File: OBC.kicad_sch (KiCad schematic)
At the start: 11 parts, among them J1 I2C, J2 Conn_02x07_Counter_Clockwise, J6 SWD, J7 RMF, SW3 SW_Push, SW5 RST, U1 E73-2G4M08S1C, Y1 32.768

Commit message: Started PCB layout
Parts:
- removed J2: Conn_02x07_Counter_Clockwise, symbol Connector_Generic:Conn_02x07_Counter_Clockwise
- added J8: GPIO, Connector_PinHeader_2.54mm:PinHeader_2x07_P2.54mm_Vertical, symbol Connector_Generic:Conn_02x07_Odd_Even
- J1: footprint (none) -> Connector_PinHeader_2.54mm:PinHeader_1x04_P2.54mm_Vertical
- L1: footprint Inductor_SMD:L_Changjiang_FTC201610D -> Inductor_SMD:L_1210_3225Metric
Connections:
- net +3.3V: now also J8.2 (Pin_2)
- net GND: now also J8.4 (Pin_4)
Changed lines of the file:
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@@
+		)
+	)
+	(global_label "RMF"
+		(shape input)
+		(at 68.58 115.57 0)
+		(fields_autoplaced yes)
+		(effects
+			(font
+				(size 1.27 1.27)
+			)
+			(justify left)
+		)
+		(property "Intersheetrefs" "${INTERSHEET_REFS}"
+			(at 75.3752 115.57 0)
+			(hide yes)
+			(show_name no)
+			(do_not_autoplace no)
+			(effects
+				(font
+					(size 1.27 1.27)
+				)
+				(justify left)
+			)
 		)
 	)
@@
 		)
 	)
+	(global_label "RMF"
+		(shape input)
+		(at 250.19 133.35 180)
+		(fields_autoplaced yes)
+		(effects
+			(font
+				(size 1.27 1.27)
+			)
+			(justify right)
+		)
+		(property "Intersheetrefs" "${INTERSHEET_REFS}"
+			(at 243.3948 133.35 0)
+			(hide yes)
+			(show_name no)
+			(do_not_autoplace no)
+			(effects
+				(font
+					(size 1.27 1.27)
+				)
+				(justify right)
+			)
+		)
+	)
 	(global_label "LoRa_SCK"
 		(shape input)
@@
 		)
 	)
-	(hierarchical_label "RMF"
-		(shape input)
-		(at 68.58 115.57 0)
-		(effects
-			(font
-				(size 1.27 1.27)
-			)
-			(justify left)
-		)
-	)
 	(hierarchical_label "{LoRa_BUS}"
 		(shape input)
@@
 			)
 			(justify left)
-		)
-	)
-	(hierarchical_label "RMF"
-		(shape input)
-		(at 250.19 133.35 180)
-		(effects
-			(font
-				(size 1.27 1.27)
-			)
-			(justify right)
 		)
 	)
@@
 	)
 	(symbol
+		(lib_id "Connector_Generic:Conn_02x07_Odd_Even")
+		(at 135.89 125.73 0)
+		(unit 1)
+		(body_style 1)
+		(exclude_from_sim no)
+		(in_bom yes)
+		(on_board yes)
+		(in_pos_files yes)
+		(dnp no)
+		(fields_autoplaced yes)
+		(property "Reference" "J8"
+			(at 137.16 111.76 0)
+			(show_name no)
+			(do_not_autoplace no)
+			(effects
+				(font
+					(size 1.27 1.27)
+				)
+			)
+		)
+		(property "Value" "GPIO"
+			(at 137.16 114.3 0)
+			(show_name no)
+			(do_not_autoplace no)
+			(effects
+				(font
+					(size 1.27 1.27)
+				)
+			)
+		)
+		(property "Footprint" "Connector_PinHeader_2.54mm:PinHeader_2x07_P2.54mm_Vertical"
+			(at 135.89 125.73 0)
+			(hide yes)
+			(show_name no)
+			(do_not_autoplace no)
+			(effects
+				(font
+					(size 1.27 1.27)
+				)
+			)
+		)
+		(property "Datasheet" ""
+			(at 135.89 125.73 0)
+			(hide yes)
+			(show_name no)
+			(do_not_autoplace no)
+			(effects
+				(font
+					(size 1.27 1.27)
+				)
+			)
+		)
+		(property "Description" "Generic connector, double row, 02x07, odd/even pin numbering scheme (row 1 odd numbers, row 2 even numbers), script generated (kicad-library-utils/schlib/autogen/connector/)"
+			(at 135.89 125.73 0)
+			(hide yes)
+			(show_name no)
+			(do_not_autoplace no)
+			(effects
+				(font
+					(size 1.27 1.27)
+				)
+			)
+		)
+		(pin "14"
+		)
+		(pin "13"
+		)
+		(pin "12"
+		)
+		(pin "11"
+		)
+		(pin "10"
+		)
+		(pin "1"
+		)
+		(pin "3"
+		)
+		(pin "2"
+		)
+		(pin "4"
+		)
+		(pin "6"
+		)
+		(pin "7"
+		)
+		(pin "5"
+		)
+		(pin "9"
+		)
+		(pin "8"
+		)
+		(instances
+			(project "CanSat_Devboard"
+				(path "/f9e05184-c88b-4a88-ae9c-ab2bdb32be7c/5d00bd0a-3bbf-46b2-b8c5-f75441fb4350/2028456c-6ef4-4d71-987d-d023cb9d3da5"
+					(reference "J8")
+					(unit 1)
+				)
+			)
+		)
+	)
+	(symbol
 		(lib_id "power:GND")
 		(at 256.54 100.33 90)
@@
 			)
 		)
-		(property "Footprint" "Inductor_SMD:L_Changjiang_FTC201610D"
+		(property "Footprint" "Inductor_SMD:L_1210_3225Metric"
 			(at 73.66 127 0)
 			(hide yes)
@@
 			)
 		)
-		(property "Footprint" ""
+		(property "Footprint" "Connector_PinHeader_2.54mm:PinHeader_1x04_P2.54mm_Vertical"
 			(at 191.77 127 0)
 			(hide yes)
@@
 					(unit 1)
 				)
-			)
-		)
-	)
-	(symbol
-		(lib_id "Connector_Generic:Conn_02x07_Counter_Clockwise")
-		(at 135.89 125.73 0)
-		(unit 1)
-		(body_style 1)
-		(exclude_from_sim no)
-		(in_bom yes)
-		(on_board yes)
-		(in_pos_files yes)
-		(dnp no)
-		(fields_autoplaced yes)
-		(property "Reference" "J2"
-			(at 137.16 111.76 0)
-			(show_name no)
-			(do_not_autoplace no)
-			(effects
-				(font
-					(size 1.27 1.27)
-				)
-			)
-		)
-		(property "Value" "Conn_02x07_Counter_Clockwise"
-			(at 137.16 114.3 0)
-			(show_name no)
-			(do_not_autoplace no)
-			(effects
-				(font
-					(size 1.27 1.27)
-				)
-			)
-		)
-		(property "Footprint" ""
-			(at 135.89 125.73 0)
-			(hide yes)
-			(show_name no)
-			(do_not_autoplace no)
-			(effects
-				(font
-					(size 1.27 1.27)
-				)
-			)
-		)
-		(property "Datasheet" ""
-			(at 135.89 125.73 0)
-			(hide yes)
-			(show_name no)
-			(do_not_autoplace no)
-			(effects
-				(font
-					(size 1.27 1.27)
-				)
-			)
-		)
-		(property "Description" "Generic connector, double row, 02x07, counter clockwise pin numbering scheme (similar to DIP package numbering), script generated (kicad-library-utils/schlib/autogen/connector/)"
-			(at 135.89 125.73 0)
-			(hide yes)
-			(show_name no)
-			(do_not_autoplace no)
-			(effects
-				(font
-					(size 1.27 1.27)
-				)
-			)
-		)
-		(pin "1"
-		)
-		(pin "12"
-		)
-		(pin "2"
-		)
-		(pin "6"
-		)
-		(pin "7"
-		)
-		(pin "14"
-		)
-		(pin "3"
-		)
-		(pin "8"
-		)
-		(pin "9"
-		)
-		(pin "5"
-		)
-		(pin "13"
-		)
-		(pin "11"
-		)
-		(pin "4"
-		)
-		(pin "10"
-		)
-		(instances
-			(project "CanSat_Devboard"
-				(path "/f9e05184-c88b-4a88-ae9c-ab2bdb32be7c/5d00bd0a-3bbf-46b2-b8c5-f75441fb4350/2028456c-6ef4-4d71-987d-d023cb9d3da5"
-					(reference "J2")
-					(unit 1)
-				)

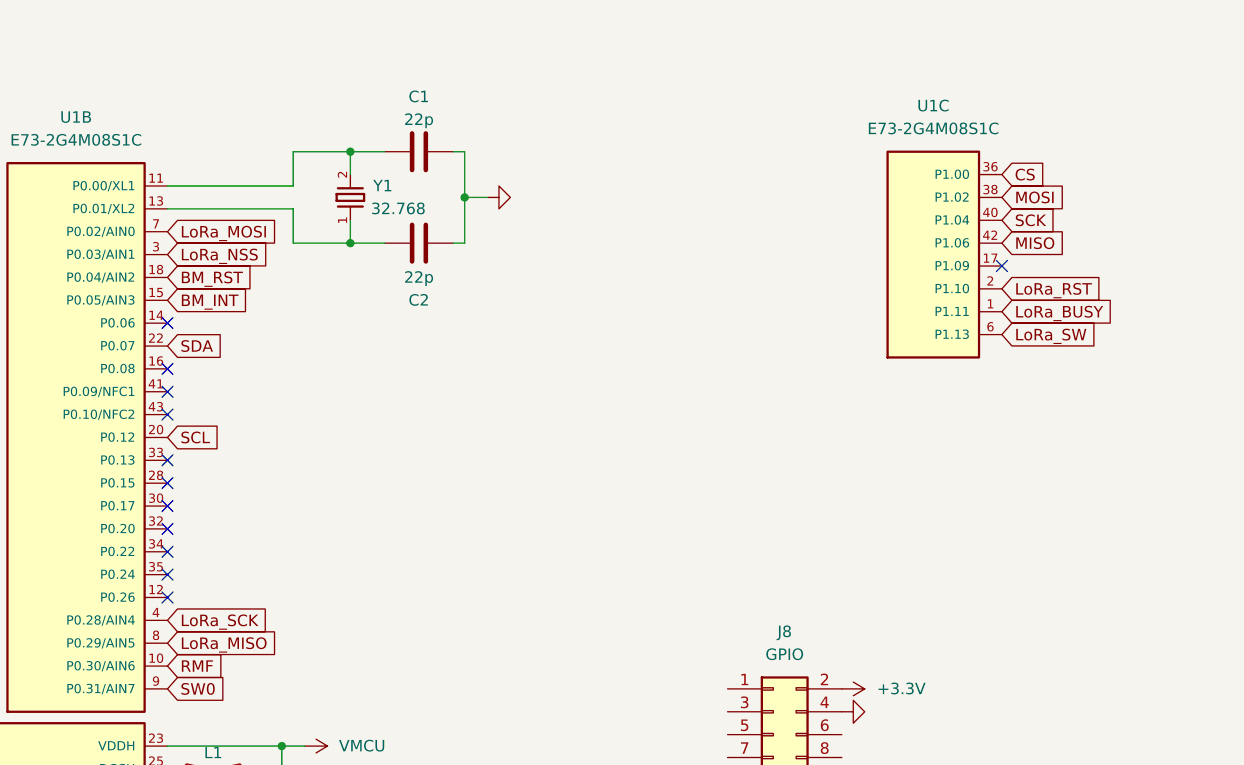
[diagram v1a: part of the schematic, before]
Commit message: Started layout
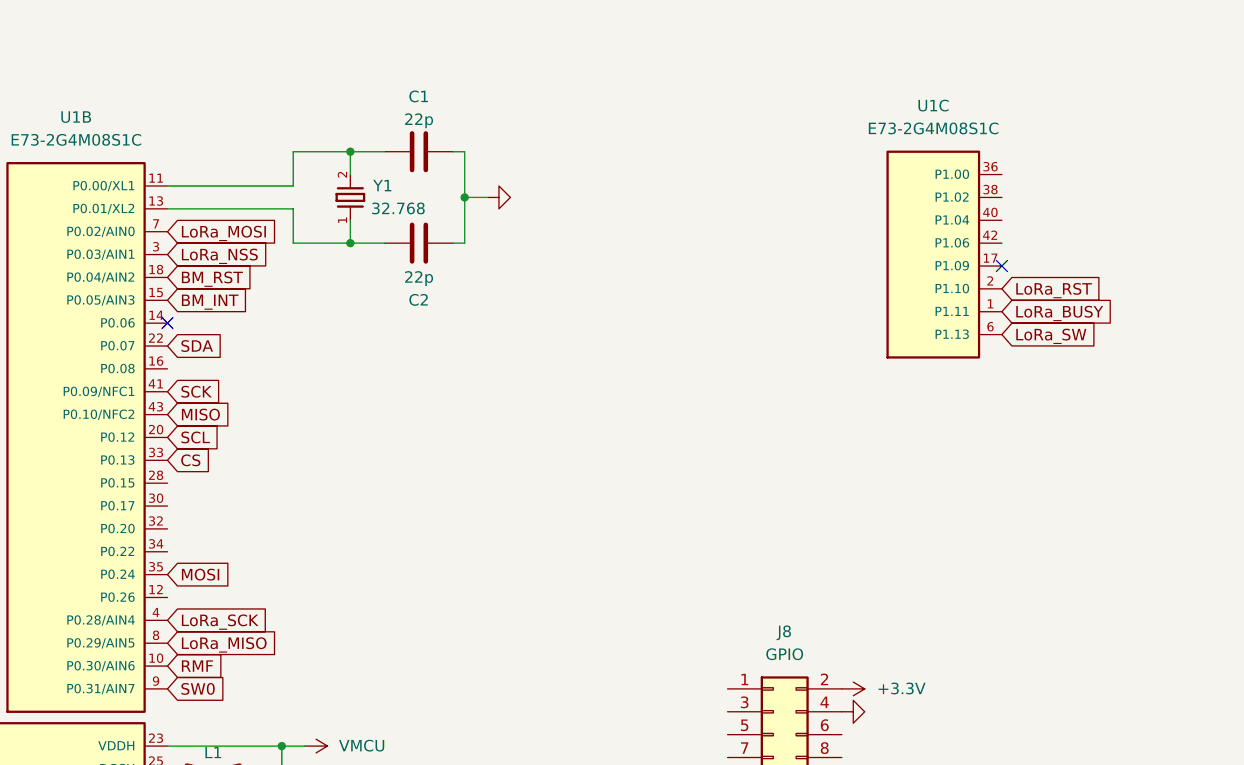
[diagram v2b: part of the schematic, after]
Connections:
- net CS: now also U1.33 (P0.13); no longer U1.36 (P1.00)
- net MISO: now also U1.43 (P0.10/NFC2); no longer U1.42 (P1.06)
- net MOSI: now also U1.35 (P0.24); no longer U1.38 (P1.02)
- net SCK: now also U1.41 (P0.09/NFC1); no longer U1.40 (P1.04)
- no-connect marks 13 -> 3
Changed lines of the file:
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@@
-	)
-	(no_connect
-		(at 68.58 92.71)
-	)
-	(no_connect
-		(at 68.58 107.95)
 	)
 	(no_connect
@@
 	)
 	(no_connect
-		(at 68.58 95.25)
-	)
-	(no_connect
 		(at 161.29 71.12)
-	)
-	(no_connect
-		(at 68.58 100.33)
-	)
-	(no_connect
-		(at 68.58 82.55)
 	)
 	(no_connect
 		(at 256.54 119.38)
 	)
-	(no_connect
-		(at 68.58 87.63)
-	)
-	(no_connect
-		(at 68.58 102.87)
-	)
-	(no_connect
-		(at 68.58 105.41)
-	)
-	(no_connect
-		(at 68.58 85.09)
-	)
-	(no_connect
-		(at 68.58 97.79)
-	)
 	(bus_entry
 		(at 217.17 46.99)
@@
 	(global_label "MOSI"
 		(shape input)
-		(at 161.29 63.5 0)
-		(fields_autoplaced yes)
-		(effects
-			(font
-				(size 1.27 1.27)
-			)
-			(justify left)
-		)
-		(property "Intersheetrefs" "${INTERSHEET_REFS}"
-			(at 168.8714 63.5 0)
+		(at 68.58 105.41 0)
+		(fields_autoplaced yes)
+		(effects
+			(font
+				(size 1.27 1.27)
+			)
+			(justify left)
+		)
+		(property "Intersheetrefs" "${INTERSHEET_REFS}"
+			(at 76.1614 105.41 0)
 			(hide yes)
 			(show_name no)
@@
 	(global_label "MISO"
 		(shape input)
-		(at 161.29 68.58 0)
-		(fields_autoplaced yes)
-		(effects
-			(font
-				(size 1.27 1.27)
-			)
-			(justify left)
-		)
-		(property "Intersheetrefs" "${INTERSHEET_REFS}"
-			(at 168.8714 68.58 0)
+		(at 68.58 87.63 0)
+		(fields_autoplaced yes)
+		(effects
+			(font
+				(size 1.27 1.27)
+			)
+			(justify left)
+		)
+		(property "Intersheetrefs" "${INTERSHEET_REFS}"
+			(at 76.1614 87.63 0)
 			(hide yes)
 			(show_name no)
@@
 	(global_label "SCK"
 		(shape input)
-		(at 161.29 66.04 0)
-		(fields_autoplaced yes)
-		(effects
-			(font
-				(size 1.27 1.27)
-			)
-			(justify left)
-		)
-		(property "Intersheetrefs" "${INTERSHEET_REFS}"
-			(at 168.0247 66.04 0)
+		(at 68.58 85.09 0)
+		(fields_autoplaced yes)
+		(effects
+			(font
+				(size 1.27 1.27)
+			)
+			(justify left)
+		)
+		(property "Intersheetrefs" "${INTERSHEET_REFS}"
+			(at 75.3147 85.09 0)
 			(hide yes)
 			(show_name no)
@@
 	(global_label "CS"
 		(shape input)
-		(at 161.29 60.96 0)
-		(fields_autoplaced yes)
-		(effects
-			(font
-				(size 1.27 1.27)
-			)
-			(justify left)
-		)
-		(property "Intersheetrefs" "${INTERSHEET_REFS}"
-			(at 166.7547 60.96 0)
-			(hide yes)
-			(show_name no)
+		(at 68.58 92.71 0)
+		(fields_autoplaced yes)
+		(effects
+			(font
+				(size 1.27 1.27)
+			)
+			(justify left)
+		)
+		(property "Intersheetrefs" "${INTERSHEET_REFS}"
+			(at 74.0447 92.71 0)
+			(hide yes)
+			(show_name no)

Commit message: Continued layout and routing
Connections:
- net BM_RST: now also U1.17 (P1.09); no longer U1.18 (P0.04/AIN2)
- net LoRa_MISO: now also U1.3 (P0.03/AIN1); no longer U1.8 (P0.29/AIN5)
- net LoRa_MOSI: now also U1.4 (P0.28/AIN4); no longer U1.7 (P0.02/AIN0)
- net LoRa_NSS: now also U1.8 (P0.29/AIN5); no longer U1.3 (P0.03/AIN1)
- net LoRa_RST: now also U1.7 (P0.02/AIN0); no longer U1.2 (P1.10)
- net LoRa_SCK: now also U1.6 (P1.13); no longer U1.4 (P0.28/AIN4)
- net LoRa_SW: now also U1.2 (P1.10); no longer U1.6 (P1.13)
- net RMF: now also U1.32 (P0.20); no longer U1.10 (P0.30/AIN6)
- net SCL: now also U1.10 (P0.30/AIN6); no longer U1.20 (P0.12)
- net SDA: now also U1.9 (P0.31/AIN7); no longer U1.22 (P0.07)
- net SW0: now also U1.34 (P0.22); no longer U1.9 (P0.31/AIN7)
- no-connect marks 3 -> 2

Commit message: Finished PCB design
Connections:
- net +3.3V: now also J1.1 (Pin_1), J8.1 (Pin_1); no longer J1.3 (Pin_3), J8.2 (Pin_2)
- net GND: now also J1.2 (Pin_2), J8.2 (Pin_2); no longer J1.4 (Pin_4), J8.4 (Pin_4)
- net RMF: now also U1.14 (P0.06); no longer U1.32 (P0.20)
- net SCL: now also J1.4 (Pin_4); no longer J1.1 (Pin_1)
- net SDA: now also J1.3 (Pin_3); no longer J1.2 (Pin_2)
- net SW0: now also U1.12 (P0.26); no longer U1.34 (P0.22)
- net 0.08: now reaches U1.16 (P0.08)
- net 0.08: now also J8.14 (Pin_14)
- net 0.04: now reaches U1.18 (P0.04/AIN2)
- net 0.04: now also J8.13 (Pin_13)
- net 0.12: now reaches U1.20 (P0.12)
- net 0.12: now also J8.12 (Pin_12)
- net 0.07: now reaches U1.22 (P0.07)
- net 0.07: now also J8.11 (Pin_11)
- net 0.15: now reaches U1.28 (P0.15)
- net 0.15: now also J8.10 (Pin_10)
- net 0.17: now reaches U1.30 (P0.17)
- net 0.17: now also J8.9 (Pin_9)
- net 1.06: now reaches J8.3 (Pin_3)
- net 1.06: now also U1.42 (P1.06)
- net 1.02: now reaches J8.5 (Pin_5)
- net 1.02: now also U1.38 (P1.02)
- net 1.00: now reaches J8.6 (Pin_6)
- net 1.00: now also U1.36 (P1.00)
- net 0.22: now reaches J8.7 (Pin_7)
- net 0.22: now also U1.34 (P0.22)
- net 0.20: now reaches J8.8 (Pin_8)
- net 0.20: now also U1.32 (P0.20)
- net 1.04: now reaches U1.40 (P1.04)
- net 1.04: now also J8.4 (Pin_4)
- no-connect marks 2 -> 1

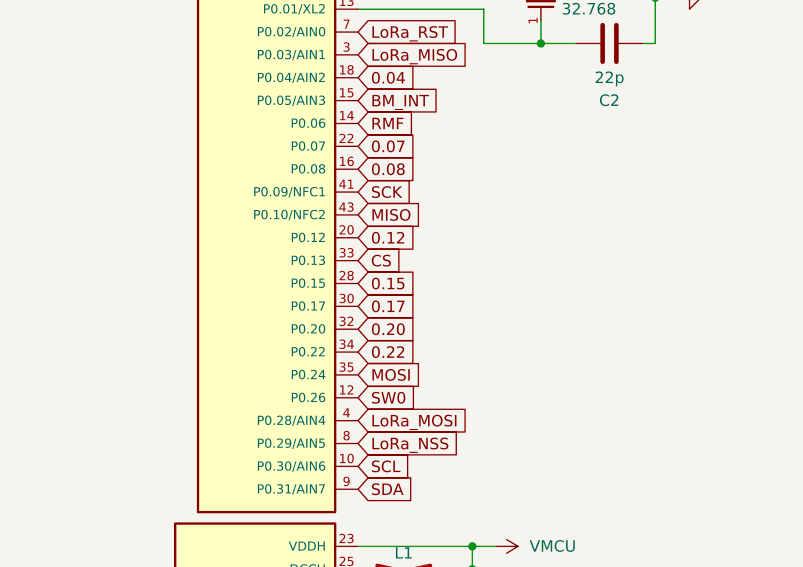
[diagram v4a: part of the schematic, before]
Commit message: Flipped SD card slot
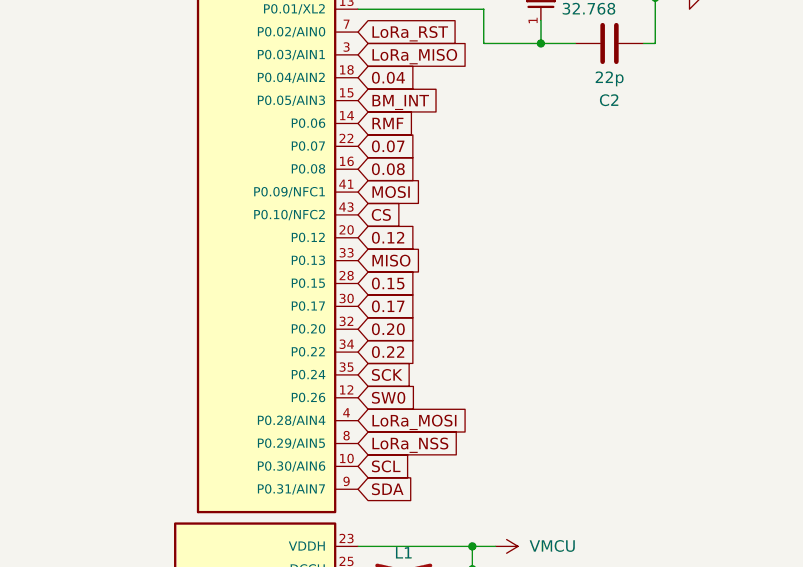
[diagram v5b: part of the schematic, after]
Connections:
- net CS: now also U1.43 (P0.10/NFC2); no longer U1.33 (P0.13)
- net MISO: now also U1.33 (P0.13); no longer U1.43 (P0.10/NFC2)
- net MOSI: now also U1.41 (P0.09/NFC1); no longer U1.35 (P0.24)
- net SCK: now also U1.35 (P0.24); no longer U1.41 (P0.09/NFC1)

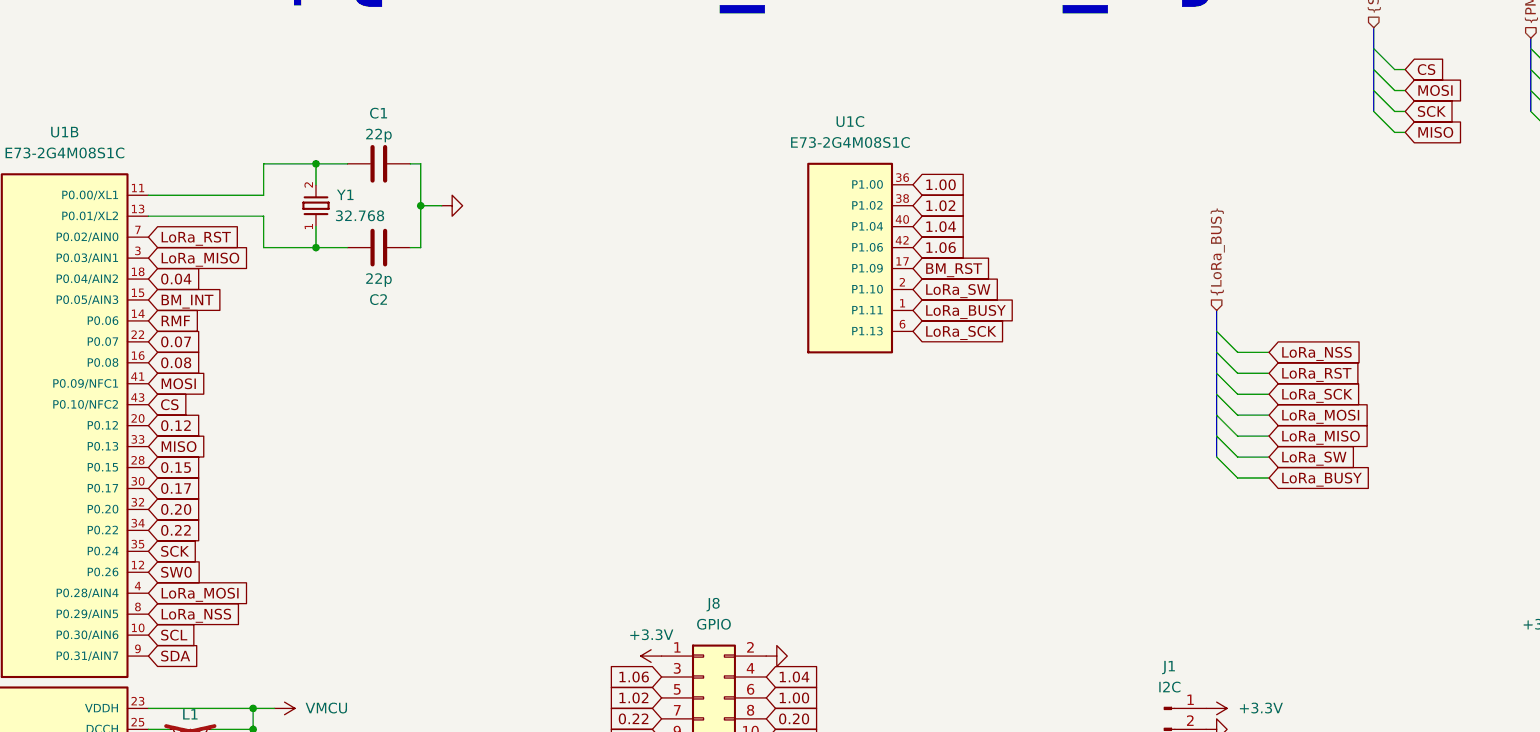
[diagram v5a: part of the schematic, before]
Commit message: Connected DIO1 of lora module
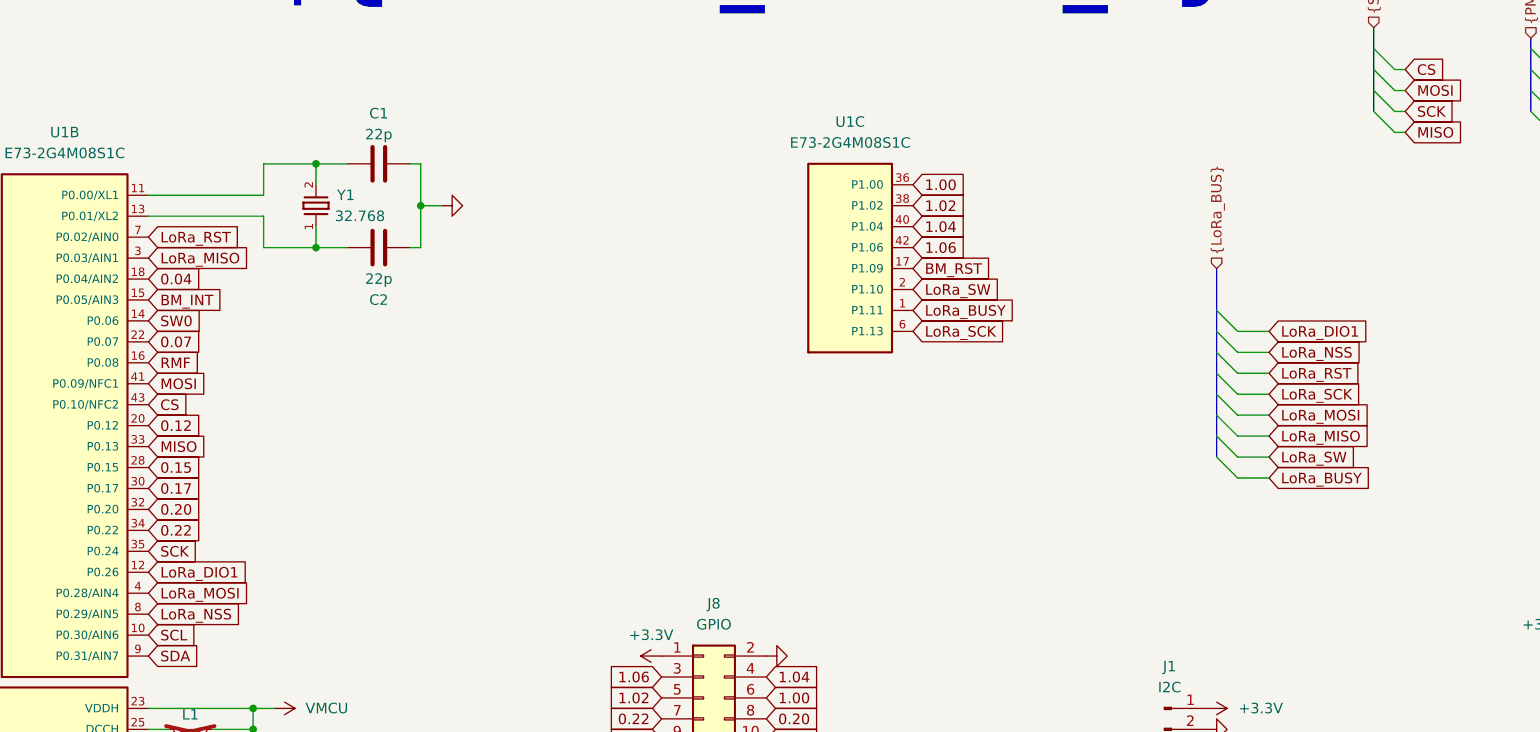
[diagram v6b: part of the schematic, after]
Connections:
- net 0.08: no longer U1.16 (P0.08)
- net RMF: now also U1.16 (P0.08); no longer U1.14 (P0.06)
- net SW0: now also U1.14 (P0.06); no longer U1.12 (P0.26)
- new net LoRa_DIO1: U1.12 (P0.26)
